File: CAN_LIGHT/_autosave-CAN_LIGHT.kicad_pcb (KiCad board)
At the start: 2 copper layers, 135.5 x 115.4 mm, 93 parts, among them J1 Conn_ARM_SWD_TagConnect_TC2030

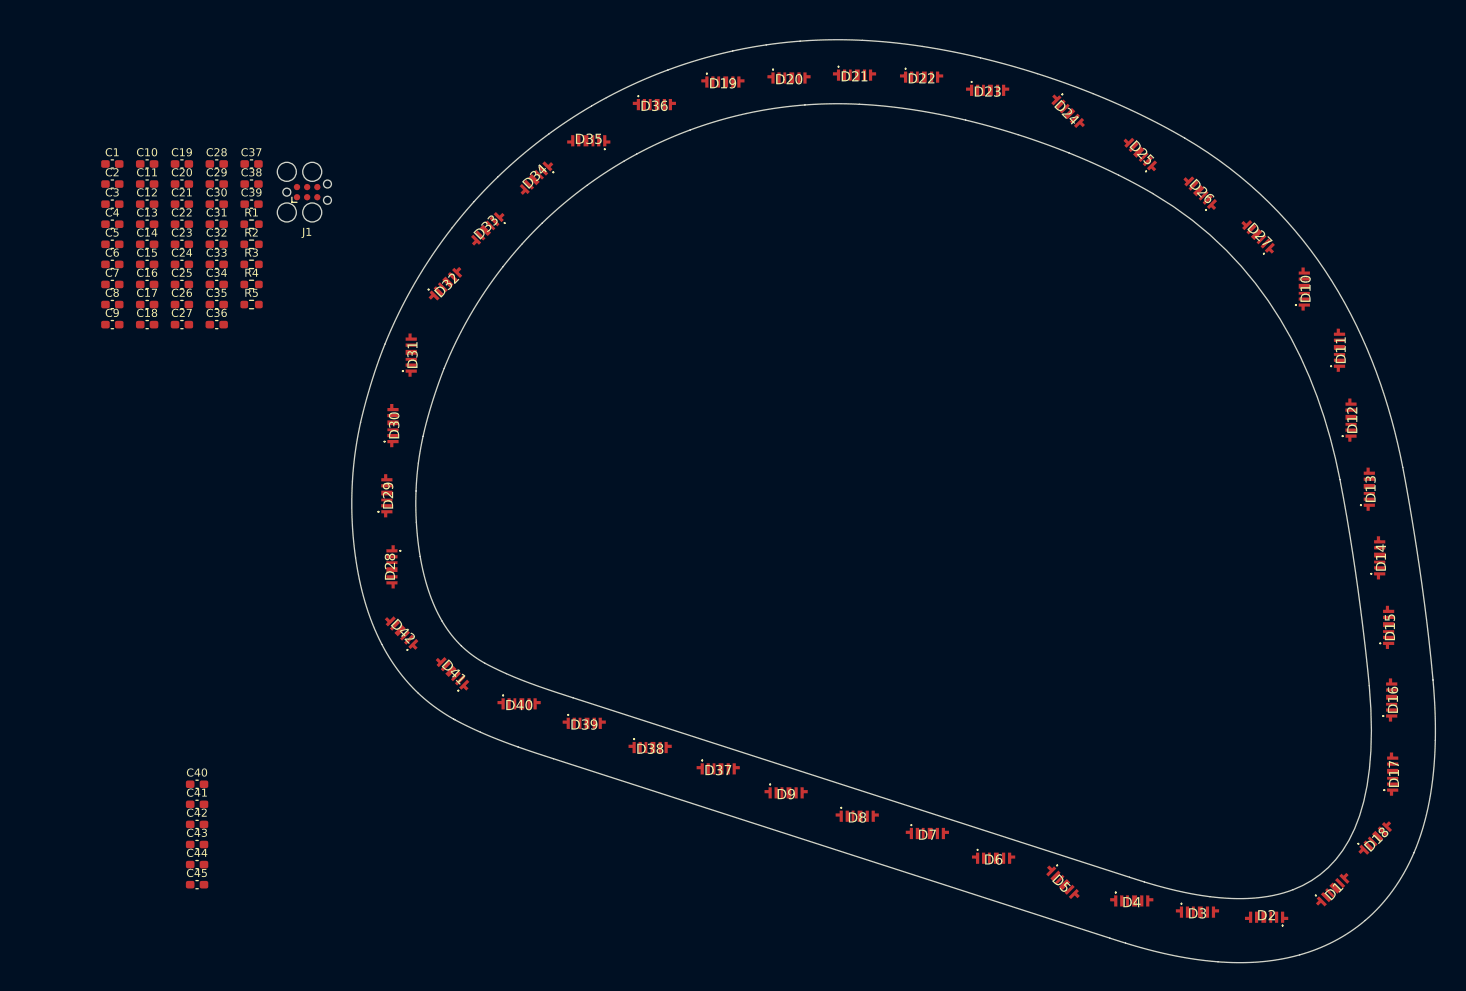
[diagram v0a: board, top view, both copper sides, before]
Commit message: Export initial STEP file to print
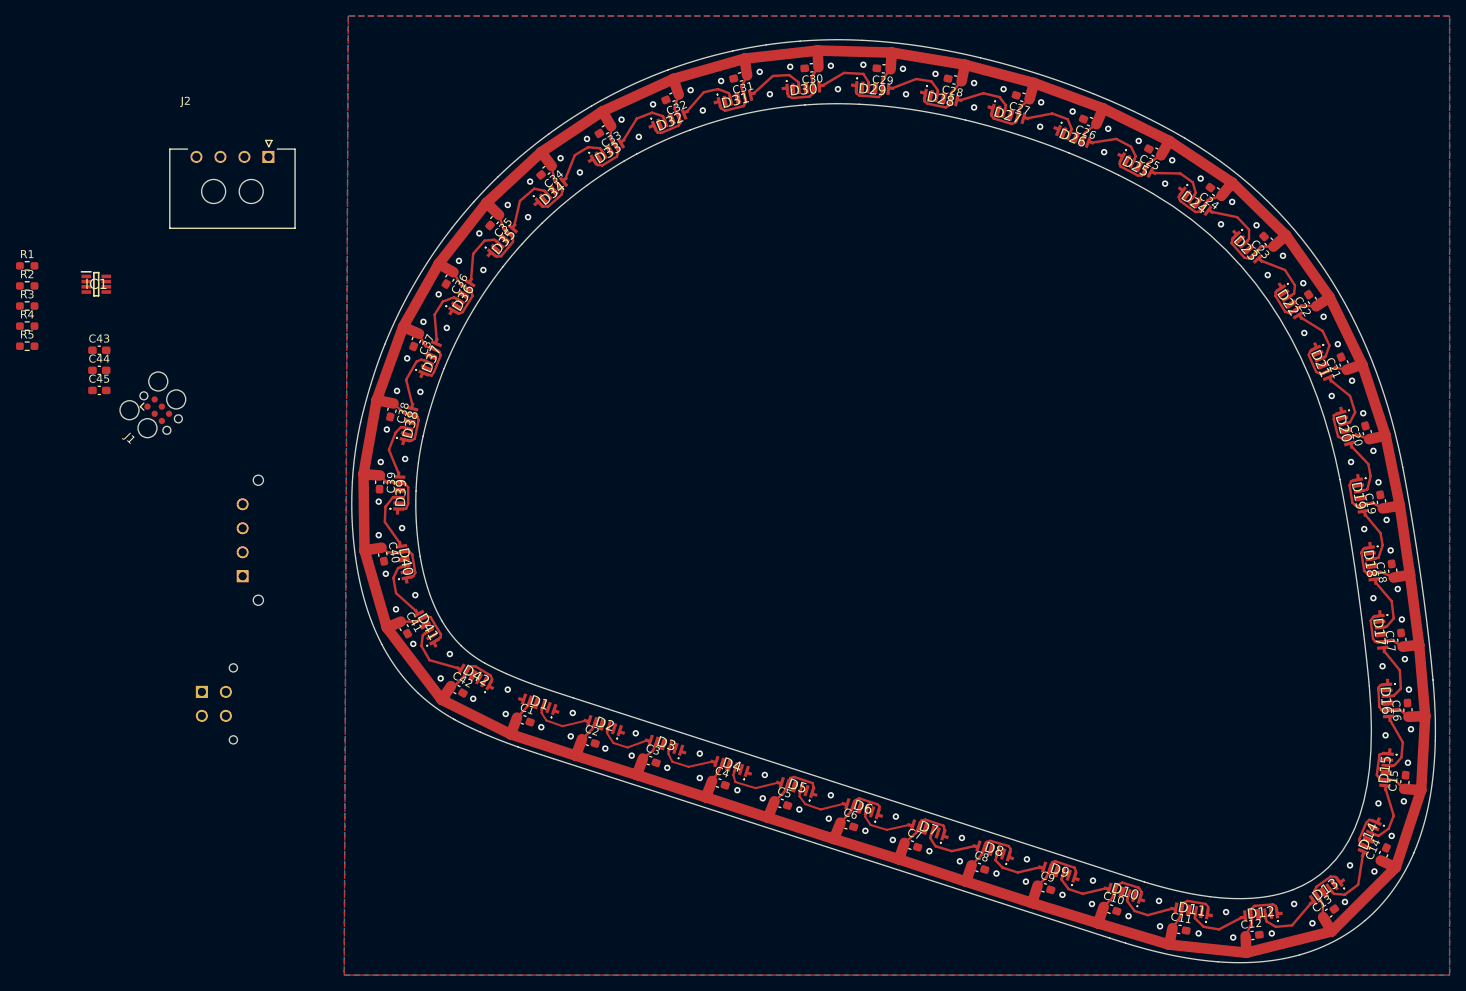
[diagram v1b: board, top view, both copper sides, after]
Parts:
- added IC1: MSPM0C1103SDDFR, MSPM0C1103SDDFR:SOT65P280X110-8N, F.Cu at (34.0, 58.3)
- added J2: 436500401, 436500401:MOLEX_436500401, F.Cu at (55.6, 42.4)
- added J3: 436500428, 436500428:CON_436500428_MOL, B.Cu at (52.3, 94.8)
- added J4: 430450428, 430450428:CON_430450428_MOL, B.Cu at (47.2, 109.3)
- C1: value 10uF -> 0.1uF
- C3: value 10nF -> 0.1uF
- C43: value 0.1uF -> 10uF
- C45: value 0.1uF -> 10nF
- R4: value 301K -> 169K
- R5: value 169K -> 301K
- moved C14 172.3 mm to (194.9, 129.5), turned to 66 degrees
- moved C13 171.0 mm to (188.1, 136.9), turned to 35.5 degrees
- moved C15 170.0 mm to (197.6, 120.5), turned to 84 degrees
- moved C16 166.3 mm to (198.0, 111.5), turned to 93.5 degrees
- moved C12 165.7 mm to (178.6, 139.7), turned to 6 degrees
- moved C17 162.3 mm to (197.2, 102.7), turned to 96.5 degrees
- moved C11 159.1 mm to (169.4, 138.9), turned to -10 degrees
- moved C18 158.7 mm to (196.1, 94.1), turned to 98.5 degrees
- moved C19 155.8 mm to (194.7, 85.5), turned to 100.5 degrees
- moved C10 152.2 mm to (160.8, 136.4), turned to -18 degrees
- moved C20 151.4 mm to (192.9, 76.8), turned to 105.75 degrees
- moved C21 146.6 mm to (190.0, 68.2), turned to 113.5 degrees
- moved C22 141.6 mm to (186.1, 60.3), turned to 122.75 degrees
- moved C9 136.1 mm to (152.5, 133.7), turned to -18 degrees
- moved C23 135.9 mm to (180.6, 53.0), turned to 133 degrees
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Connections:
- C1 pad 1: +3.3V -> +5V
- C2 pad 1: +3.3V -> +5V
- C3 pad 1: Net-(IC1-PA1_/_NRST) -> +5V
- C43 pad 1: +5V -> +3.3V
- C44 pad 1: +5V -> +3.3V
- C45 pad 1: +5V -> Net-(IC1-PA1_/_NRST)
- D11 pad 6: Net-(D11-DIN) -> Net-(D10-DOUT)
- D20 pad 6: Net-(D20-DIN) -> Net-(D19-DOUT)
- D21 pad 6: Net-(D21-DIN) -> Net-(D20-DOUT)
- D22 pad 6: Net-(D19-DOUT) -> Net-(D21-DOUT)
- D23 pad 6: Net-(D20-DOUT) -> Net-(D22-DOUT)
- D24 pad 6: Net-(D21-DOUT) -> Net-(D23-DOUT)
- D25 pad 6: Net-(D22-DOUT) -> Net-(D24-DOUT)
- D26 pad 6: Net-(D23-DOUT) -> Net-(D25-DOUT)
- D27 pad 6: Net-(D24-DOUT) -> Net-(D26-DOUT)
- D28 pad 6: Net-(D25-DOUT) -> Net-(D27-DOUT)
- D29 pad 6: Net-(D26-DOUT) -> Net-(D28-DOUT)
- D30 pad 6: Net-(D27-DOUT) -> Net-(D29-DOUT)
- D31 pad 6: Net-(D28-DOUT) -> Net-(D30-DOUT)
- D32 pad 6: Net-(D29-DOUT) -> Net-(D31-DOUT)
- D33 pad 6: Net-(D30-DOUT) -> Net-(D32-DOUT)
- D34 pad 3: Net-(D20-DIN) -> Net-(D34-DOUT)
- D34 pad 6: Net-(D31-DOUT) -> Net-(D33-DOUT)
- D35 pad 3: Net-(D21-DIN) -> Net-(D35-DOUT)
- D35 pad 6: Net-(D32-DOUT) -> Net-(D34-DOUT)
- D36 pad 6: Net-(D33-DOUT) -> Net-(D35-DOUT)
- D5 pad 6: Net-(D10-DOUT) -> Net-(D4-DOUT)
- D8 pad 3: Net-(D11-DIN) -> Net-(D8-DOUT)
- D9 pad 6: Net-(D4-DOUT) -> Net-(D8-DOUT)
- R4 pad 2: +3.3V -> GND
- R5 pad 2: GND -> +3.3V
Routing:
- net +5V: track 0.00 -> 776.6 mm
- net Net-(D13-DOUT): track 0.00 -> 8.04 mm
- net Net-(D12-DOUT): track 0.00 -> 7.98 mm
- net Net-(D41-DOUT): track 0.00 -> 7.97 mm
- net Net-(D14-DOUT): track 0.00 -> 7.70 mm
- net Net-(D40-DOUT): track 0.00 -> 7.58 mm
- net Net-(D22-DOUT): track 0.00 -> 7.56 mm
- net Net-(D11-DOUT): track 0.00 -> 7.52 mm
- net Net-(D30-DOUT): track 0.00 -> 7.51 mm
- net Net-(D35-DOUT): track 0.00 -> 7.51 mm
- net Net-(D23-DOUT): track 0.00 -> 7.48 mm
- net Net-(D37-DOUT): track 0.00 -> 7.47 mm
- net Net-(D34-DOUT): track 0.00 -> 7.46 mm
- net Net-(D16-DOUT): track 0.00 -> 7.43 mm
- net Net-(D25-DOUT): track 0.00 -> 7.43 mm
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- added copper zone on B.Cu, net GND
- added copper zone on F.Cu, net GND
